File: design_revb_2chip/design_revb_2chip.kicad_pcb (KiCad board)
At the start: 4 copper layers, 101.5 x 50.5 mm, 102 parts, among them J1 USB_C_Receptacle, J2 Conn_01x08, J3 09452812810, U1 LAN7801-I/9JX, U2 TPS62162QDSGRQ1, U3 93C56A-I/P, U4 DP83TG720SWRHARQ1, U5 TPS784105QWDRBRQ1

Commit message: USB_Side Prelim Completion
- finished USB side with no revisions
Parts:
- added U6: 219-5MST, Capstone_Footprints:SW5_219SMT, F.Cu at (231.7, 83.9)
- C12, C4: moved to B.Cu
- moved J2 25.0 mm to (215.0, 99.0)
- moved C12 2.69 mm to (200.3, 76.0)
- moved C3 2.69 mm to (198.0, 83.3)
- moved C2 2.50 mm to (195.5, 83.5), turned to 0 degrees
- moved C4 2.38 mm to (199.8, 73.5)
- moved C6 1.16 mm to (195.2, 82.5), turned to 0 degrees
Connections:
- net Net-(J1-RX1+) renamed /USB_SIDE/USB3_RXP
- net Net-(J1-RX1-) renamed /USB_SIDE/USB3_RXN
- net Net-(J1-TX1+) renamed /USB_SIDE/USB3_TXP
- net Net-(J1-TX1-) renamed /USB_SIDE/USB3_TXN
- net Net-(U1-USB2_DM) renamed /USB_SIDE/USB2_N
- net Net-(U1-USB2_DP) renamed /USB_SIDE/USB2_P
- C21 pad 1: 3.3V -> VDD33A
- C30 pad 1: Vdd -> VDD33A
- C32 pad 1: Vdd -> VDD33A
- C33 pad 2: Vdd -> VDD33A
- C34 pad 2: Vdd -> VDD33A
- D2 pad 2: 3.3V -> VDD33A
- D3 pad 1: Net-(D3-K) -> /ETH_SIDE/LED_0_STRP_ON
- D5 pad 2: Net-(D5-A) -> /ETH_SIDE/LED_0_STRP_OFF
- J2 pad 1: GPIO4 -> GPIO10
- J2 pad 2: GPIO5 -> GPIO9
- J2 pad 3: GPIO6 -> GPIO8
- J2 pad 5: GPIO8 -> GPIO6
- J2 pad 6: GPIO9 -> GPIO5
- J2 pad 7: GPIO10 -> GPIO4
- L2 pad 2: 3.3V -> VDD33A
- R11 pad 2: 3.3V -> VDD33A
- R21 pad 1: Net-(D3-K) -> /ETH_SIDE/LED_0_STRP_ON
- R21 pad 2: Vdd -> VDD33A
- R23 pad 2: Vdd -> VDD33A
- R26 pad 1: Net-(D5-A) -> /ETH_SIDE/LED_0_STRP_OFF
- R27 pad 1: Vdd -> VDD33A
- R27 pad 2: Net-(JP3-B) -> /ETH_SIDE/RX_D0_STRP
- R28 pad 1: Vdd -> VDD33A
- R28 pad 2: Net-(JP4-B) -> /ETH_SIDE/RX_D1_STRP
- R29 pad 1: Vdd -> VDD33A
- R29 pad 2: Net-(JP5-B) -> /ETH_SIDE/RX_D2_STRP
- R9 pad 2: 3.3V -> VDD33A
- U2 pad 6: 3.3V -> VDD33A
- U4 pad 24: /ETH_SIDE/RX_D2_STRP -> /ETH_SIDE/RX_D2_DIP
- U4 pad 25: /ETH_SIDE/RX_D1_STRP -> /ETH_SIDE/RX_D1_DIP
- U4 pad 26: /ETH_SIDE/RX_D0_STRP -> /ETH_SIDE/RX_D0_DIP
- U4 pad 35: /ETH_SIDE/LED_0 -> /ETH_SIDE/LED_0_DIP
- U5 pad 8: Vdd -> VDD33A
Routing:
- net GPIO5: track 0.00 -> 64.8 mm, vias 0 -> 2
- net GPIO4: track 0.00 -> 63.9 mm, vias 0 -> 2
- net GPIO6: track 0.00 -> 52.6 mm
- net VDD33A: track 111.5 -> 155.8 mm, vias 14 -> 15
- net GPIO10: track 0.00 -> 36.2 mm
- net GPIO9: track 0.00 -> 35.1 mm
- net GPIO8: track 0.00 -> 34.5 mm
- net GPIO7: track 0.00 -> 33.6 mm
- net 3.3V: track 33.5 -> 0.00 mm, vias 1 -> 0
- net /USB_SIDE/PHY_RESET_N: track 0.00 -> 30.3 mm, vias 0 -> 1
- net /USB_SIDE/PHY_INT_N: track 0.00 -> 28.1 mm, vias 0 -> 1
- net /USB_SIDE/USB3_TXN: track 0.00 -> 27.6 mm
- net /USB_SIDE/USB3_TXP: track 0.00 -> 27.5 mm
- net /USB_SIDE/USB2_P: track 0.00 -> 27.0 mm, vias 0 -> 2
- net /USB_SIDE/USB2_N: track 0.00 -> 26.9 mm, vias 0 -> 2
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- added copper zone on In2.Cu, net VDD33A
- removed copper zone on In2.Cu, net 3.3V

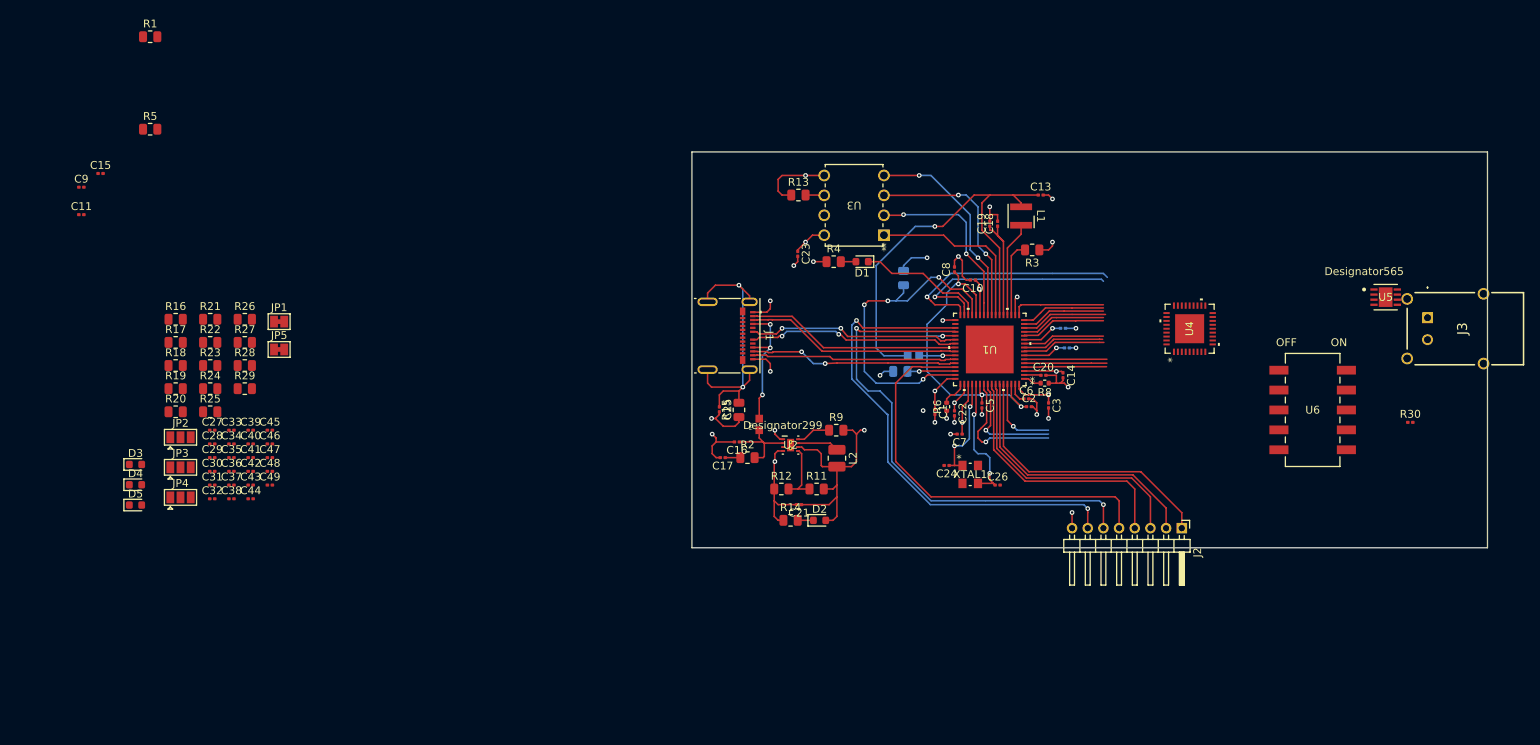
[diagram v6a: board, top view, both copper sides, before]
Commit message: routing eth side
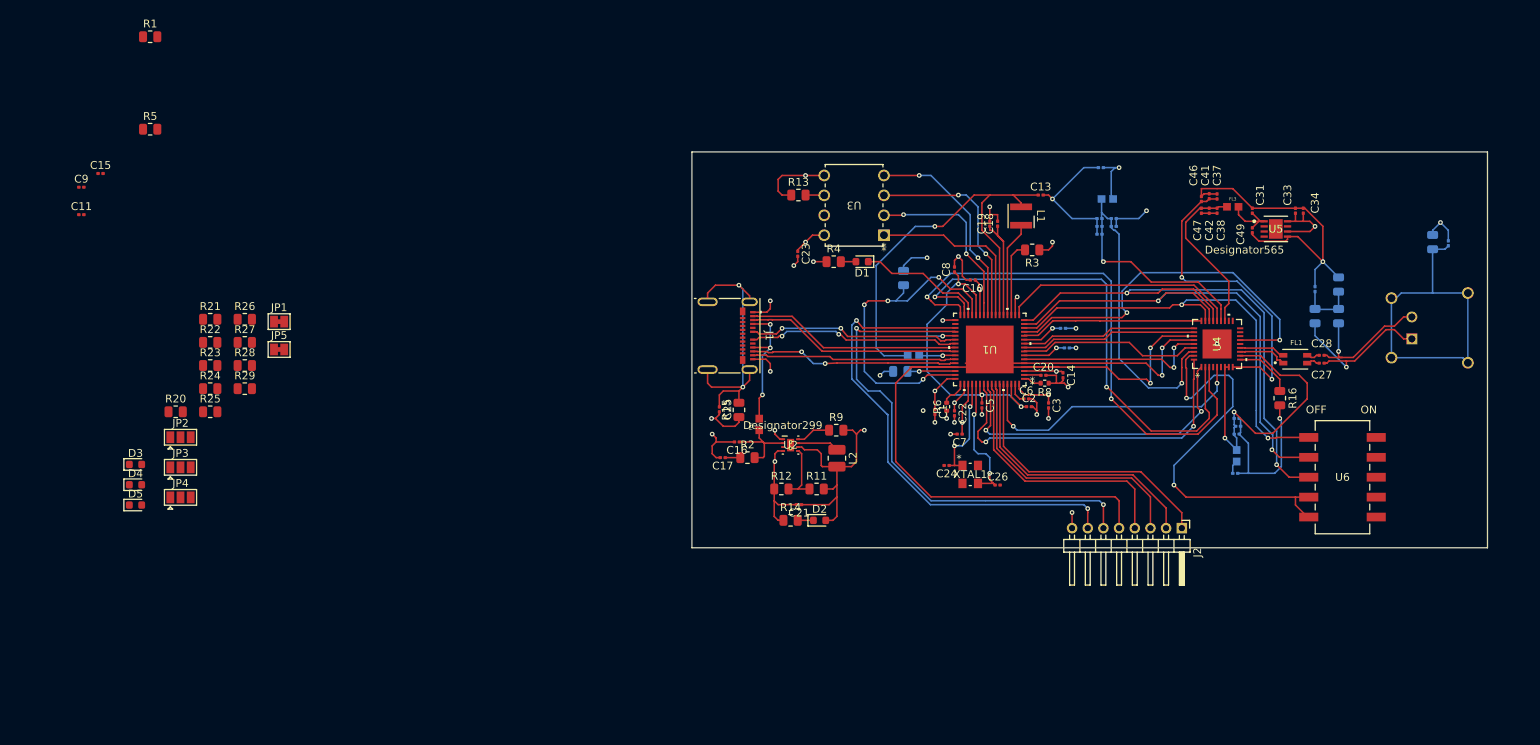
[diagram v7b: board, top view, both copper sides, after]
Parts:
- added C50: 0.1uF, Capacitor_SMD:C_0201_0603Metric, B.Cu at (249.0, 62.7)
- added FL1: DLW32MH101XT2L, Capstone_Footprints:FIL_DLW32MH101XT2L, F.Cu at (229.5, 77.4)
- added FL2: BLM18KG601SH1D, Capstone_Footprints:BEADC1608X95N, B.Cu at (205.5, 57.0)
- added FL3: BLM18KG601SH1D, Capstone_Footprints:BEADC1608X95N, F.Cu at (221.5, 58.0)
- added FL4: BLM18KG601SH1D, Capstone_Footprints:BEADC1608X95N, B.Cu at (222.0, 89.8)
- C29, C30, C32, C35, C36, C39, C40, C43, C44, C45, C48, J3, R17, R18, R19: moved to B.Cu
- R30: footprint Capacitor_SMD:C_0201_0603Metric -> Resistor_SMD:R_0805_2012Metric; moved to B.Cu
- moved R19 149.0 mm to (235.0, 67.9), turned to 90 degrees
- moved R18 148.5 mm to (235.0, 71.9), turned to 90 degrees
- moved R17 145.4 mm to (232.0, 71.9), turned to 90 degrees
- moved C29 142.3 mm to (232.0, 68.5), turned to 90 degrees
- moved C28 142.0 mm to (232.8, 76.9), turned to 180 degrees
- moved C27 141.8 mm to (232.8, 77.9)
- moved R16 141.2 mm to (227.5, 82.4), turned to -90 degrees
- moved C34 139.9 mm to (230.5, 58.5), turned to -90 degrees
- moved C33 138.6 mm to (229.5, 58.5), turned to -90 degrees
- moved C31 137.2 mm to (224.0, 58.5), turned to 90 degrees
- moved C37 131.0 mm to (219.5, 56.7), turned to -90 degrees
- moved C38 131.0 mm to (219.5, 58.5), turned to -90 degrees
- moved C32 130.6 mm to (221.8, 92.0)
- moved C49 129.5 mm to (224.0, 61.0), turned to 90 degrees
- moved C41 126.8 mm to (218.5, 56.7), turned to -90 degrees
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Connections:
- C27 pad 1: Net-(C27-Pad1) -> /ETH_SIDE/BI_DA+
- C27 pad 2: Net-(J3-BI_DA+) -> /ETH_SIDE/BI_DA+
- C28 pad 1: Net-(J3-BI_DA+) -> /ETH_SIDE/BI_DA-
- C28 pad 2: Net-(C28-Pad2) -> /ETH_SIDE/BI_DA-
- J3 pad 1: Net-(J3-BI_DA+) -> /ETH_SIDE/BI_DA+
- J3 pad 2: Net-(J3-BI_DA+) -> /ETH_SIDE/BI_DA-
- R1 pad 1: /USB_SIDE/MDIO -> MDIO
- R17 pad 1: Net-(J3-BI_DA+) -> /ETH_SIDE/BI_DA+
- R18 pad 1: Net-(J3-BI_DA+) -> /ETH_SIDE/BI_DA-
- R20 pad 2: /ETH_SIDE/MDIO -> MDIO
- U1 pad 10: /USB_SIDE/TXC -> TXC
- U1 pad 12: /USB_SIDE/RXC -> RXC
- U1 pad 13: /USB_SIDE/RX_CTL -> RX_CTL
- U1 pad 14: /USB_SIDE/RXD0 -> RXD0
- U1 pad 15: /USB_SIDE/RXD1 -> RXD1
- U1 pad 16: /USB_SIDE/RXD2 -> RXD2
- U1 pad 17: /USB_SIDE/RXD3 -> RXD3
- U1 pad 31: /USB_SIDE/PHY_INT_N -> PHY_INT_N
- U1 pad 32: /USB_SIDE/PHY_RESET_N -> PHY_RESET_N
- U1 pad 4: /USB_SIDE/TXD3 -> TXD3
- U1 pad 5: /USB_SIDE/TXD2 -> TXD2
- U1 pad 55: /USB_SIDE/MDIO -> MDIO
- U1 pad 56: /USB_SIDE/MDC -> MDC
- U1 pad 6: /USB_SIDE/TXD1 -> TXD1
- U1 pad 61: /USB_SIDE/REF_25CLK -> REF_25CLK
- U1 pad 8: /USB_SIDE/TXD0 -> TXD0
- U1 pad 9: /USB_SIDE/TX_CTL -> TX_CTL
- U4 pad 1: /ETH_SIDE/MDC -> MDC
- U4 pad 13: /ETH_SIDE/TRD_M -> /ETH_SIDE/TRD_N
- U4 pad 15: /ETH_SIDE/RX_CTL -> RX_CTL
- U4 pad 2: /ETH_SIDE/PHY_INT_N -> PHY_INT_N
- U4 pad 23: /ETH_SIDE/RXD3 -> RXD3
- U4 pad 24: /ETH_SIDE/RX_D2_DIP -> RXD2
- U4 pad 25: /ETH_SIDE/RX_D1_DIP -> RXD1
- U4 pad 26: /ETH_SIDE/RX_D0_DIP -> RXD0
- U4 pad 27: /ETH_SIDE/RXC -> RXC
- U4 pad 28: /ETH_SIDE/TXC -> TXC
- U4 pad 29: /ETH_SIDE/TX_CTL -> TX_CTL
- U4 pad 3: /ETH_SIDE/PHY_RESET_N -> PHY_RESET_N
- U4 pad 30: /ETH_SIDE/TXD3 -> TXD3
- U4 pad 31: /ETH_SIDE/TXD2 -> TXD2
- U4 pad 32: /ETH_SIDE/TXD1 -> TXD1
- U4 pad 33: /ETH_SIDE/TXD0 -> TXD0
- U4 pad 36: /ETH_SIDE/MDIO -> MDIO
- U4 pad 5: /ETH_SIDE/REF_25CLK -> REF_25CLK
- U5 pad 6: Vdd -> VDD33A
- U6 pad 1: /ETH_SIDE/RX_D0_DIP -> RXD0
- U6 pad 2: /ETH_SIDE/RX_D1_DIP -> RXD1
- U6 pad 3: /ETH_SIDE/RX_D2_DIP -> RXD2
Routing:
- net GND: track 109.4 -> 269.8 mm, vias 24 -> 29
- net VDD33A: track 155.8 -> 267.2 mm, vias 15 -> 17
- net RXD2: track 0.00 -> 72.0 mm, vias 0 -> 2
- net PHY_RESET_N: track 0.00 -> 68.9 mm, vias 0 -> 2
- net RXD1: track 0.00 -> 65.0 mm, vias 0 -> 2
- net PHY_INT_N: track 0.00 -> 64.6 mm, vias 0 -> 2
- net /ETH_SIDE/VddioA: track 0.00 -> 62.2 mm, vias 0 -> 2
- net /ETH_SIDE/Vdd1p0A: track 0.00 -> 61.3 mm, vias 0 -> 2
- net RXD0: track 0.00 -> 57.7 mm, vias 0 -> 2
- net /ETH_SIDE/LED_0_DIP: track 0.00 -> 51.4 mm, vias 0 -> 2
- net RX_CTL: track 0.00 -> 48.3 mm, vias 0 -> 2
- net TXD3: track 0.00 -> 46.7 mm, vias 0 -> 2
- net MDIO: track 0.00 -> 44.6 mm, vias 0 -> 2
- net Net-(J3-GND_1): track 0.00 -> 44.3 mm
- net MDC: track 0.00 -> 41.3 mm, vias 0 -> 2
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
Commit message: routing doen
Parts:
- R20, R21, R22, R24: moved to B.Cu
- moved D4 171.0 mm to (252.5, 96.5), turned to -90 degrees
- moved D3 169.1 mm to (250.5, 96.5), turned to 90 degrees
- moved D5 167.0 mm to (248.5, 96.5), turned to -90 degrees
- moved R25 160.7 mm to (251.5, 93.5), turned to 180 degrees
- moved R22 160.2 mm to (250.0, 95.5)
- moved R24 159.9 mm to (250.0, 98.5), turned to 180 degrees
- moved R26 157.0 mm to (251.5, 90.0)
- moved R23 156.3 mm to (246.0, 99.0), turned to 180 degrees
- moved R21 156.3 mm to (245.5, 96.1), turned to -90 degrees
- moved R28 149.5 mm to (244.5, 90.0), turned to 180 degrees
- moved R29 149.5 mm to (244.5, 92.5), turned to 180 degrees
- moved R27 149.5 mm to (244.4, 87.5), turned to 180 degrees
- moved R20 125.0 mm to (211.5, 89.0), turned to 180 degrees
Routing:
- net GND: track 269.8 -> 337.1 mm, vias 29 -> 31
- net /ETH_SIDE/LED_1: track 0.00 -> 65.1 mm, vias 0 -> 1
- net VDD33A: track 267.2 -> 321.5 mm, vias 17 -> 19
- net /ETH_SIDE/LED_0_STRP_ON: track 0.00 -> 20.5 mm, vias 0 -> 1
- net /ETH_SIDE/LED_0_STRP_OFF: track 0.00 -> 17.3 mm
- net Net-(D4-K): track 0.00 -> 10.8 mm, vias 0 -> 1
- net Net-(D3-A): track 0.00 -> 5.70 mm
- net /ETH_SIDE/RX_D1_STRP: track 0.00 -> 3.80 mm
- net /ETH_SIDE/RX_D2_STRP: track 0.00 -> 3.78 mm
- net /ETH_SIDE/RX_D0_STRP: track 0.00 -> 3.73 mm
- net Net-(D5-K): track 0.00 -> 3.08 mm
- net MDIO: track 44.6 -> 47.3 mm
- net /ETH_SIDE/BI_DA+: track 23.2 -> 25.6 mm
- net Net-(J3-GND_1): track 44.3 -> 45.1 mm
- net /ETH_SIDE/BI_DA-: track 20.1 -> 20.9 mm
